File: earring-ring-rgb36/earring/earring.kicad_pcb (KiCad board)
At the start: 4 copper layers, 25 x 27.3 mm, 44 parts, among them J1 Conn_01x04, SW1 SW_Push, U2 STM32L031G6Ux

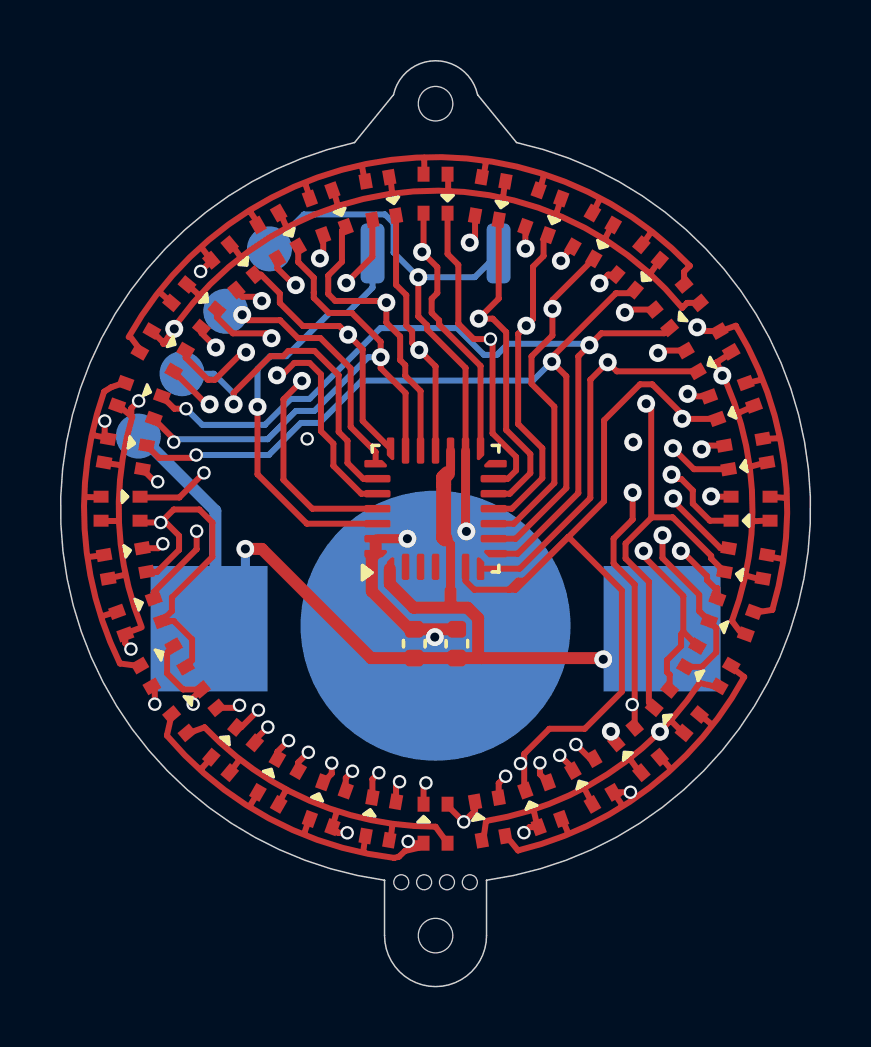
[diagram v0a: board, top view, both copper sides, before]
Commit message: earring-ring-rgb36: various fixes
* Fix problem: A9 and SWDIO were swapped
* Change program header to use a different order of pins
* various small fixes
* remove fp-info-cache which doesn't need to be committed
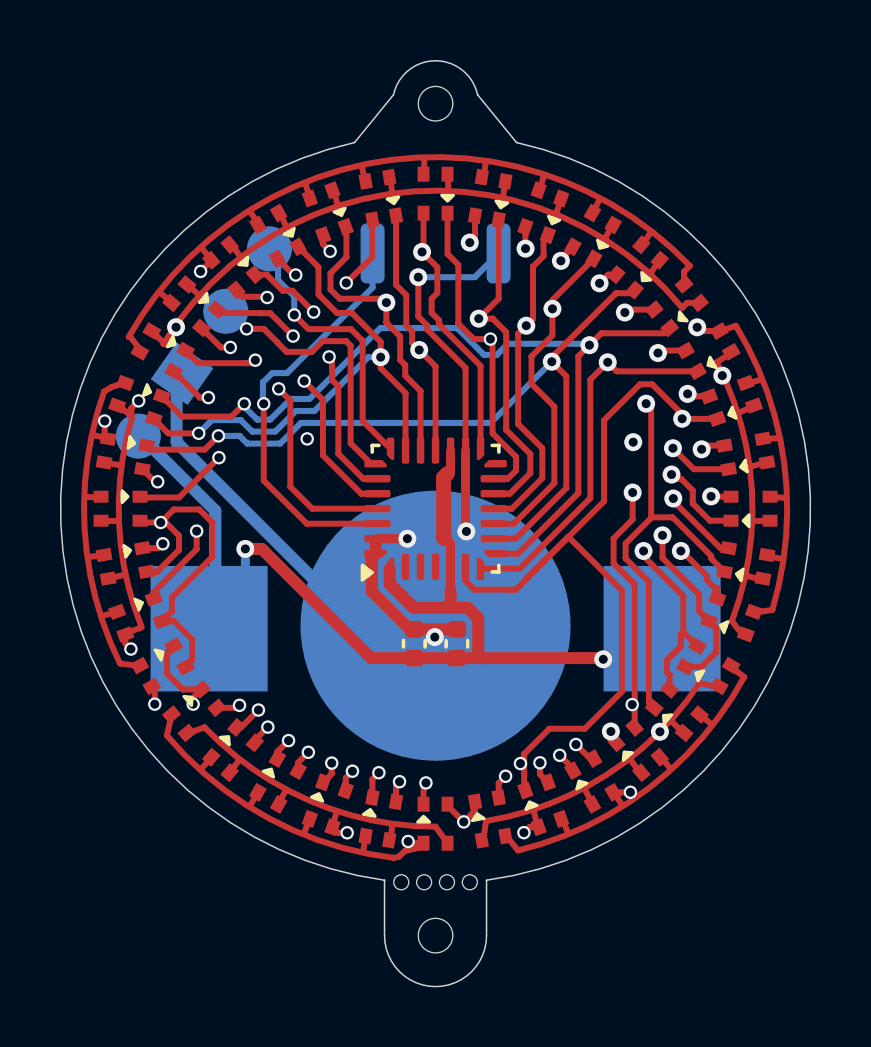
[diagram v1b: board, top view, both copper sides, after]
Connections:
- J1 pad 2: SWDIO -> GND
- J1 pad 4: GND -> SWDIO
- U2 pad 21: A9 -> SWDIO
- U2 pad 23: SWDIO -> A9
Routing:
- net GND: track 35.1 -> 41.7 mm
- net SWDIO: track 11.4 -> 9.17 mm
- net B1: track 14.1 -> 12.5 mm
- net A8: track 53.9 -> 52.7 mm
- net G1: track 14.0 -> 13.0 mm
- net A7: track 52.2 -> 51.2 mm
- net A9: track 48.7 -> 49.6 mm, vias 4 -> 5
- net A10: track 54.5 -> 55.3 mm
- net SWCLK: track 8.48 -> 9.30 mm
- net Net-(U2-PB7): track 14.3 -> 13.8 mm
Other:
- board text added: "LED earring v0.2"
- board text removed: "36-LED earring v0.1"

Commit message: earring-ring-rgb36: small changes
* use a single capacitor instead of two (apparently that's just fine)
* add a NRST test point
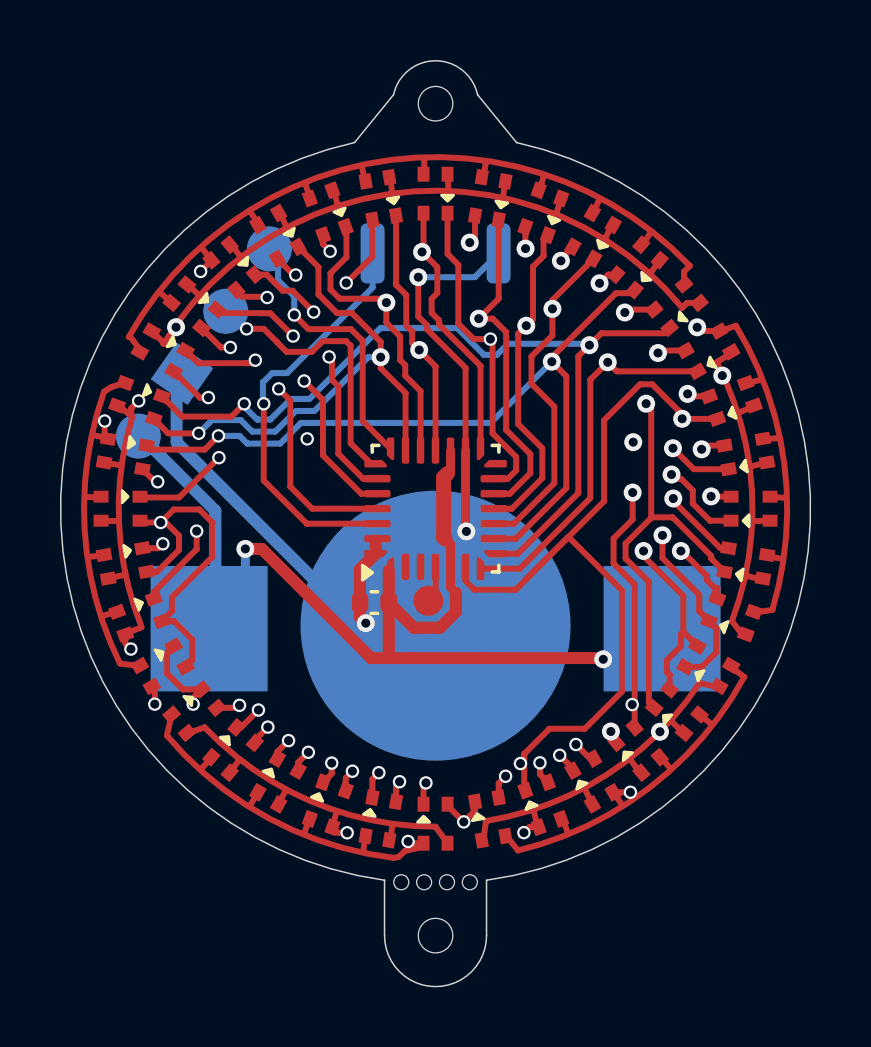
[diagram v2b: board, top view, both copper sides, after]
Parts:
- removed C1: 100nF, Capacitor_SMD:C_0402_1005Metric
- added TP1: TestPoint_Small, Custom:TestPoint_1.0x1.0mm, F.Cu at (-0.24, 3.07)
- moved C2 1.91 mm to (-2.04, 3.13), turned to 180 degrees
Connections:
- U2 pad 4: unconnected-(U2-NRST-Pad4) -> Net-(U2-NRST)
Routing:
- net GND: track 41.7 -> 28.8 mm, vias 4 -> 3
- net Net-(U2-NRST): track 0.00 -> 1.23 mm
- net VCC: track 37.6 -> 38.4 mm
